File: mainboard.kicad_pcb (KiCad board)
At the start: 2 copper layers, 220.9 x 240.6 mm, 77 parts, among them J1 DRV8833-1, J10 Conn_02x04_Counter_Clockwise, J11 Conn_02x04_Counter_Clockwise, J12 Conn_02x04_Counter_Clockwise, J13 Conn_PCA9685, J14 Conn_01x02, J15 Conn_01x02, J16 Conn_01x02, J17 Conn_02x04_Counter_Clockwise, J18 Screw_Terminal_01x06, J19 Screw_Terminal_01x06, J2 DRV8833-0, J20 Screw_Terminal_01x06, J21 Screw_Terminal_01x06, J22 Screw_Terminal_01x06, J23 Screw_Terminal_01x06, J24 Screw_Terminal_01x04, J25 Screw_Terminal_01x02, J26 Conn_02x04_Counter_Clockwise, J3 Conn_01x02, J4 Screw_Terminal_01x06, J5 Screw_Terminal_01x06, J6 VIM4_HEADER, J7 Screw_Terminal_01x06, J8 Screw_Terminal_01x06, J9 Conn_02x04_Counter_Clockwise, Q3 2N7000, Q4 2N7000, SW1 RotaryEncoder_Switch, SW3 SW_SPST, U1 MCP23017_SP

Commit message: First full buildup for the PCB
Board1, bucks removed. Motor interface added,
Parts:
- removed C1, C2: 1uF, Capacitor_SMD:C_0805_2012Metric
- removed the C10 at (274.9, 42.2)
- removed the C5 at (127.3, 116.0)
- removed the C8 at (274.9, 36.2)
- removed the C9 at (274.9, 39.2)
- removed D1: LED_Small, LED_SMD:LED_0805_2012Metric_Pad1.15x1.40mm_HandSolder
- removed F1, F2, F3, F4, F5, F6: Fuse, Fuse:Fuseholder_Clip-5x20mm_Schurter_CQM_Inline_P20.60x5.00mm_D1.00mm_Horizontal
- removed J10, J11, J12, J17, J26, J9: Conn_02x04_Counter_Clockwise, Connector_PinHeader_2.54mm:PinHeader_2x04_P2.54mm_Vertical
- removed the J14 at (275.0, 29.8)
- removed the J15 at (279.6, 29.8)
- removed the J16 at (284.2, 29.8)
- removed the J3 at (123.5, 108.7)
- removed the J3 at (223.5, 97.0)
- removed the R11 at (219.0, 102.1)
- removed the R11 at (270.5, 29.0)
- removed the R12 at (270.5, 32.0)
- removed the R13 at (270.5, 34.9)
- removed the R14 at (270.5, 37.9)
- removed the R15 at (270.5, 40.8)
- removed the R16 at (270.5, 43.8)
- removed the R6 at (119.7, 113.5)
- removed the R7 at (123.5, 116.0)
- removed R9: LDR07, OptoDevice:R_LDR_5.1x4.3mm_P3.4mm_Vertical
- removed SW1: RotaryEncoder_Switch, Rotary_Encoder:RotaryEncoder_Alps_EC11E-Switch_Vertical_H20mm
- removed SW3: SW_SPST, LED_SMD:LED_0805_2012Metric_Pad1.15x1.40mm_HandSolder
- added ?: , clipboard:9c2f8d19-4101-4f98-a26c-8554f3c2bdce, F.Cu at (25.5, 71.6)
- added ?: , , F.Cu at (159.3, 122.9)
- added ?: , clipboard:9c2f8d19-4101-4f98-a26c-8554f3c2bdce, F.Cu at (155.8, 29.6)
- added ?: , , F.Cu at (159.3, 120.4)
- added ?: , , F.Cu at (25.5, 74.1)
- added ?: , clipboard:9e3165f1-3c62-4009-ad41-a695cb7dbfe7, F.Cu at (159.3, 112.2)
- added ?: , clipboard:9e3165f1-3c62-4009-ad41-a695cb7dbfe7, F.Cu at (42.2, 21.2)
- added ?: , , F.Cu at (155.8, 27.1)
- added C11: 1uF, Capacitor_SMD:C_0805_2012Metric, F.Cu at (83.8, 46.3)
- added C7: 1uF, Capacitor_SMD:C_0805_2012Metric, F.Cu at (81.3, 46.3)
- added J25: Screw_Terminal_01x02, Connector_PinHeader_2.54mm:PinHeader_1x02_P2.54mm_Vertical, F.Cu at (153.5, 128.9)
- added J27: Rotary Encoder Conn, Connector_JST:JST_EH_B4B-EH-A_1x04_P2.50mm_Vertical, F.Cu at (95.4, 45.3)
- added J28: Conn_01x02, Connector_JST:JST_EH_B2B-EH-A_1x02_P2.50mm_Vertical, F.Cu at (101.8, 74.9)
- added J28: Conn_01x02, Connector_JST:JST_EH_B2B-EH-A_1x02_P2.50mm_Vertical, F.Cu at (114.7, 19.6)
- added J28: Conn_01x02, Connector_JST:JST_EH_B2B-EH-A_1x02_P2.50mm_Vertical, F.Cu at (122.7, 19.6)
- added J28: Conn_01x02, Connector_JST:JST_EH_B2B-EH-A_1x02_P2.50mm_Vertical, F.Cu at (106.8, 19.6)
- added J28: Conn_01x02, Connector_JST:JST_EH_B2B-EH-A_1x02_P2.50mm_Vertical, F.Cu at (98.7, 19.6)
- added J3: Conn_01x02, Connector_PinHeader_2.54mm:PinHeader_1x02_P2.54mm_Vertical, F.Cu at (140.6, 103.6)
- added R11: 220, Resistor_SMD:R_0805_2012Metric, F.Cu at (150.5, 45.5)
- J18, J19, J20, J21, J22, J23, J7, J8: footprint Connector_PinHeader_2.54mm:PinHeader_1x06_P2.54mm_Vertical -> TerminalBlock:TerminalBlock_Xinya_XY308-2.54-6P_1x06_P2.54mm_Horizontal
- J6: footprint Connector_IDC:IDC-Header_2x20_P2.54mm_Latch_Vertical -> Connector_IDC:IDC-Header_2x20_P2.54mm_Vertical
- moved J20 176.9 mm to (59.9, 115.9), turned to -90 degrees
- moved A2 173.4 mm to (97.6, 96.4), turned to 90 degrees
- moved J21 168.7 mm to (73.5, 116.0), turned to -90 degrees
- moved J18 160.0 mm to (60.1, 140.0), turned to -90 degrees
- moved J19 151.5 mm to (73.5, 140.1), turned to -90 degrees
- moved J22 142.3 mm to (107.5, 116.0), turned to -90 degrees
- moved J23 134.8 mm to (120.8, 116.0), turned to -90 degrees
- moved J16 119.7 mm to (136.7, 32.1), turned to 180 degrees
- moved C10 118.6 mm to (133.6, 35.0), turned to 90 degrees
- moved Q4 117.8 mm to (142.5, 29.6), turned to 180 degrees
- moved R14 117.1 mm to (133.6, 30.9), turned to -90 degrees
- moved R16 113.6 mm to (141.2, 34.0), turned to -90 degrees
- moved J7 107.1 mm to (107.3, 139.8), turned to -90 degrees
- moved J14 105.1 mm to (147.5, 29.5)
- moved Brd1 103.8 mm to (103.5, 41.2)
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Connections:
- A1 pad 31: Net-(A1-GPIO26_ADC0) -> ADC0_GP26
- A1 pad 32: Net-(A1-GPIO27_ADC1) -> ADC1_GP27
- A1 pad 34: Net-(A1-GPIO28_ADC2) -> ADC2_GP28
- A1 pad 39: unconnected-(A1-VSYS-Pad39) -> 5V_BUCK
- A1 pad 40: 5V_BUCK -> unconnected-(A1-VBUS-Pad40)_1
- A2 pad 39: unconnected-(A2-VSYS-Pad39) -> 5V_BUCK
- A2 pad 40: 5V_BUCK -> unconnected-(A2-VBUS-Pad40)
- J6 pad 31: TOTEM-EXTEND -> PIC_STATE
- J6 pad 32: PIC_STATE -> TOTEM-EXTEND
- RN1 pad 12: unconnected-(RN1-R11-Pad12) -> TOTEM-EXTEND
- RN1 pad 4: TOTEM-EXTEND -> DOOR-R
- RN1 pad 5: DOOR-R -> DOOR-L
- RN1 pad 6: DOOR-L -> CP-R
- RN1 pad 7: CP-R -> CP-L
- RN1 pad 8: CP-L -> SORT(en/dis)
- RN1 pad 9: COLL/SORT(en/dis) -> COLL(en/dis)
- U1 pad 21: COLL/SORT(en/dis) -> COLL(en/dis)
- U1 pad 22: CP-L -> SORT(en/dis)
- U1 pad 23: CP-R -> CP-L
- U1 pad 24: DOOR-L -> CP-R
- U1 pad 25: DOOR-R -> DOOR-L
- U1 pad 26: TOTEM-EXTEND -> DOOR-R
- U1 pad 3: unconnected-(U1-GPB2-Pad3) -> TOTEM-EXTEND
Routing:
- net 5V_BUCK: track 0.00 -> 399.6 mm
- net 3V_BUCK: track 0.00 -> 145.7 mm, vias 0 -> 1
- net 12V_BUCK2: track 0.00 -> 119.0 mm, vias 0 -> 1
- net 12V_BUCK3: track 0.00 -> 93.9 mm
- net CP-R-ENDSTOP0: track 0.00 -> 78.1 mm
- net PICO1_3V3: track 0.00 -> 75.7 mm
- net CP-R-ENDSTOP1: track 0.00 -> 73.0 mm
- net PCA9685_SCL: track 0.00 -> 68.3 mm
- net PCA9685_SDA: track 0.00 -> 65.3 mm
- net TOTEM-EXTEND: track 0.00 -> 63.6 mm
- net CP-L: track 0.00 -> 59.7 mm
- net GREEN: track 0.00 -> 57.4 mm
- net DOOR-L: track 0.00 -> 57.1 mm
- net CP-R: track 0.00 -> 57.1 mm
- net DOOR-R: track 0.00 -> 52.1 mm
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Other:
- board size 220.9 x 240.6 mm -> 145 x 145.9 mm
- board text added: "${REFERENCE}"
- board text added: "+"
- board text added: "-"
- board text added: "12V(1)"
- board text added: "12V(2)"
- board text added: "12V(3)"
- board text added: "3V"
- board text added: "COLL SORT"
- board text added: "CPL CPR"
- board text added: "EL0"
- board text added: "EL1"
- board text added: "ENCODER"
- board text added: "ER0"
- board text added: "ER1"
- board text added: "FRONT(L)"
- board text added: "FRONT(R)"
- board text added: "OLED"
- board text added: "PWMBUS"
- board text added: "REAR(L)"
- board text added: "REAR(R)"
- board text added: "START"
- board text added: "STOP"
- board text added: "SW G"
- board text added: "SW R"
- board text removed: "12V"
- board text removed: "3.3V"
- board text removed: "C/S"
- board text removed: "Conn_02x04_Counter_Clockwise"
- board text removed: "MC1"
- board text removed: "MC2"
- board text removed: "PICO"
- board text removed: "SWITCH/BUTTON FILTER"
- board text removed: "VIM4"

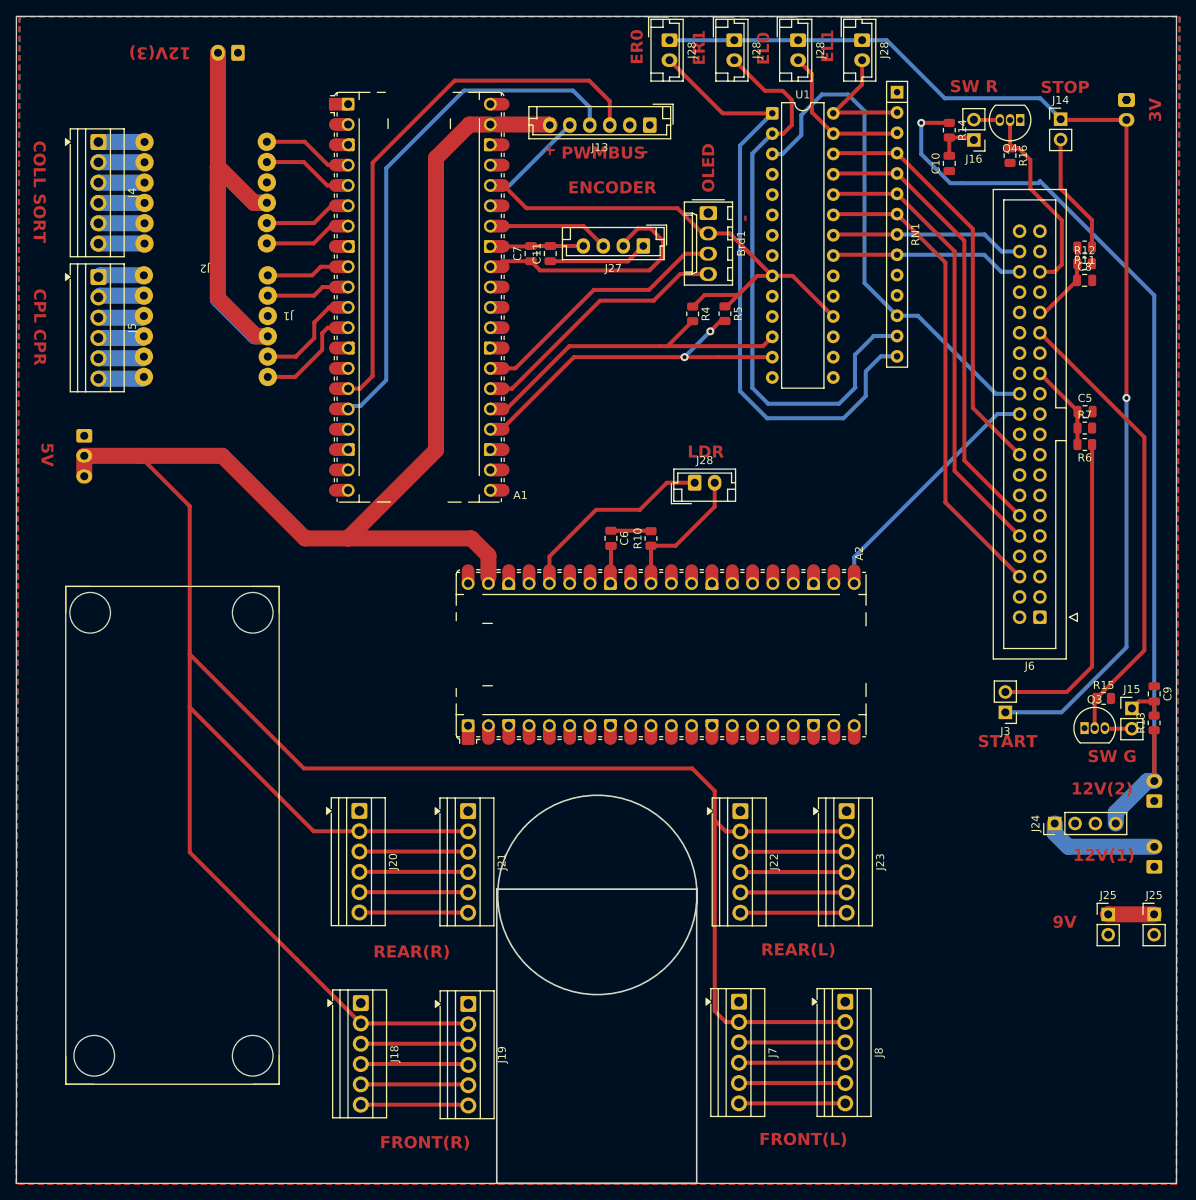
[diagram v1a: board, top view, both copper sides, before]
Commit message: 0 Error DRC mainboard V1
completed digital rules check and electrical rules check. ready to export to gerber
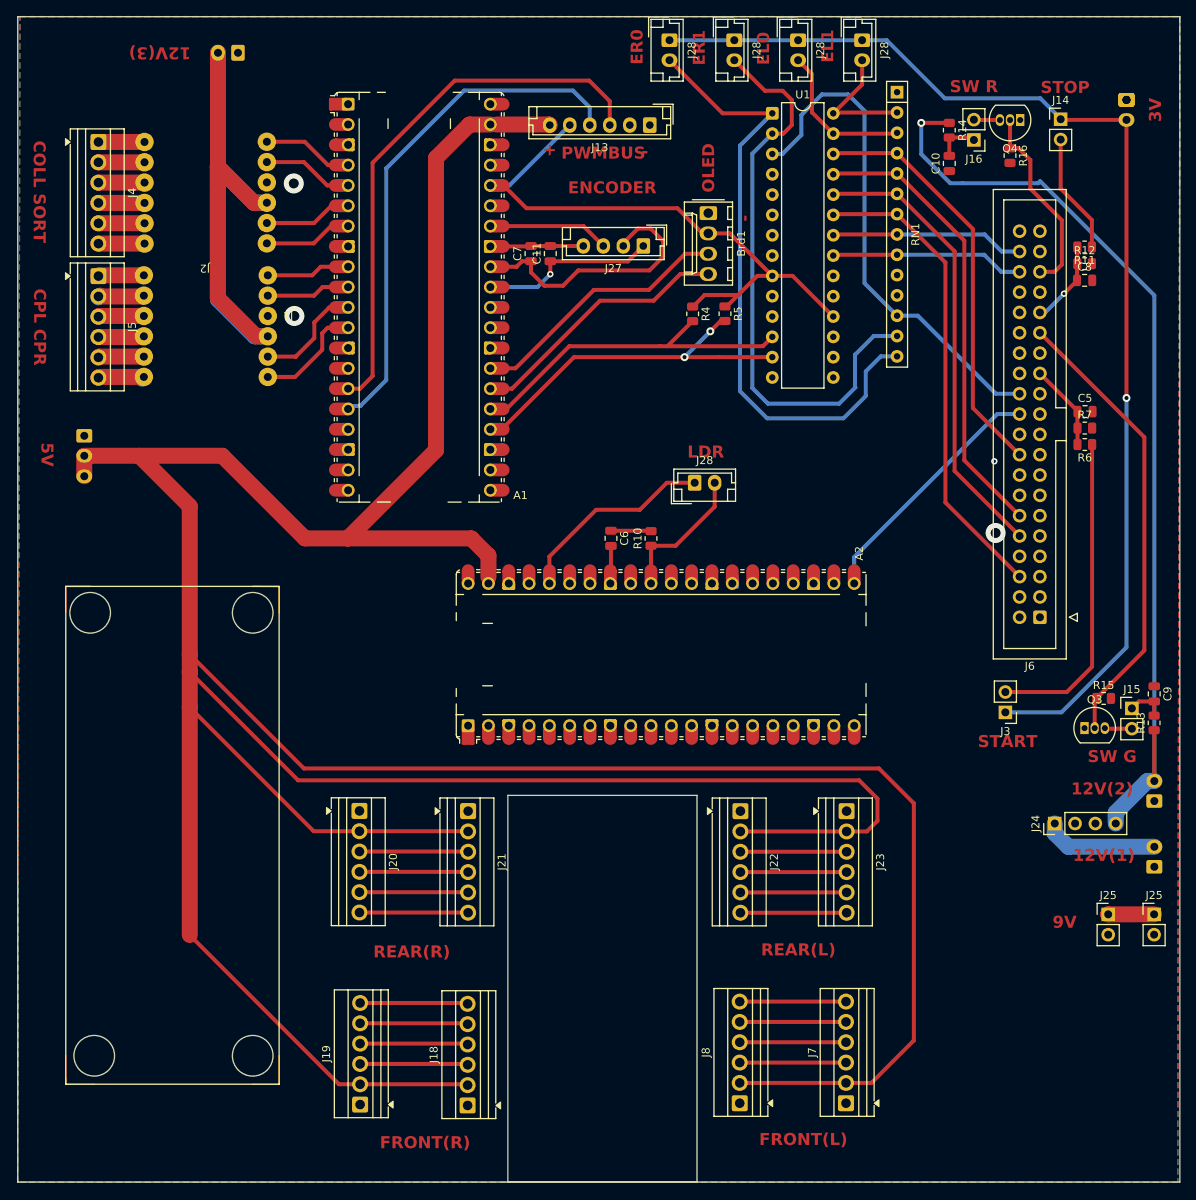
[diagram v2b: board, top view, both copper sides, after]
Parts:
- moved J18 18.5 mm to (73.4, 152.8), turned to 90 degrees
- moved J19 18.5 mm to (60.0, 152.7), turned to 90 degrees
- moved J7 18.4 mm to (120.7, 152.5), turned to 90 degrees
- moved J8 18.3 mm to (107.4, 152.5), turned to 90 degrees
- moved J5 0.12 mm to (27.3, 49.1)
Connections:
- A1 pad 17: unconnected-(A1-GPIO13-Pad17) -> unconnected-(A1-GPIO13-Pad17)_1
- A1 pad 19: unconnected-(A1-GPIO13-Pad17) -> unconnected-(A1-GPIO14-Pad19)
- A1 pad 20: unconnected-(A1-GPIO13-Pad17) -> unconnected-(A1-GPIO15-Pad20)_1
- A2 pad 10: unconnected-(A2-GPIO7-Pad10)_1 -> (no net)
- U1 pad 19: unconnected-(U1-INTA-Pad20) -> unconnected-(U1-INTB-Pad19)
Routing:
- net 5V_BUCK: track 399.6 -> 539.6 mm
- net ADC0_GP26: track 12.4 -> 22.2 mm, vias 0 -> 1
- net ADC1_GP27: track 31.0 -> 33.4 mm
- net Net-(C6-Pad1): track 6.69 -> 5.03 mm
- net STOP: track 10.5 -> 11.1 mm, vias 0 -> 1
- net GND: vias 0 -> 4
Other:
- board size 145 x 145.9 mm -> 145.3 x 145.7 mm
- board text removed: "${REFERENCE}"
